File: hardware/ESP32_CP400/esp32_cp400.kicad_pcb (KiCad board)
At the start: 2 copper layers, 110 x 60 mm, 24 parts, among them J2 USB_A, J3 USB_A, J4 USB_A, J5 Micro_SD_Card, J6 Barrel_Jack, J7 DA15_Pins

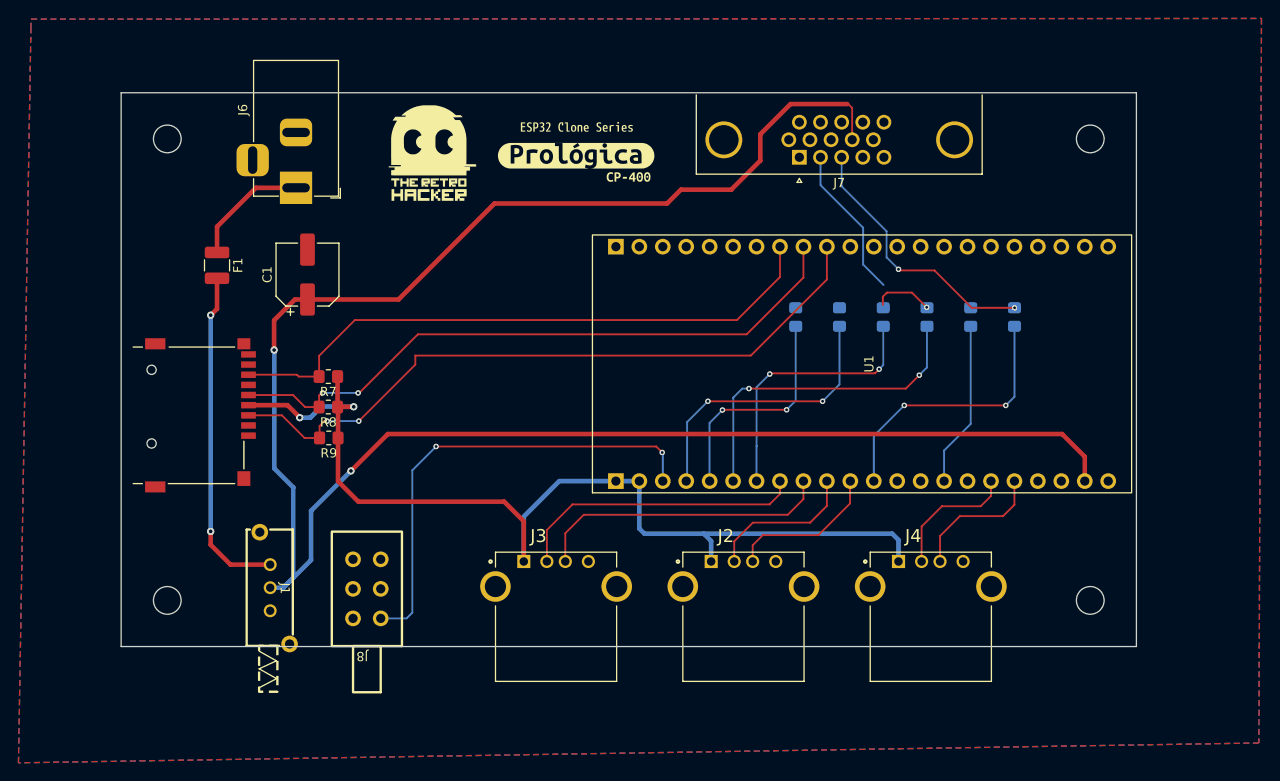
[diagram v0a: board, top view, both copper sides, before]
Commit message: Remove lock files for KiCad projects in ESP32_CP400 directory
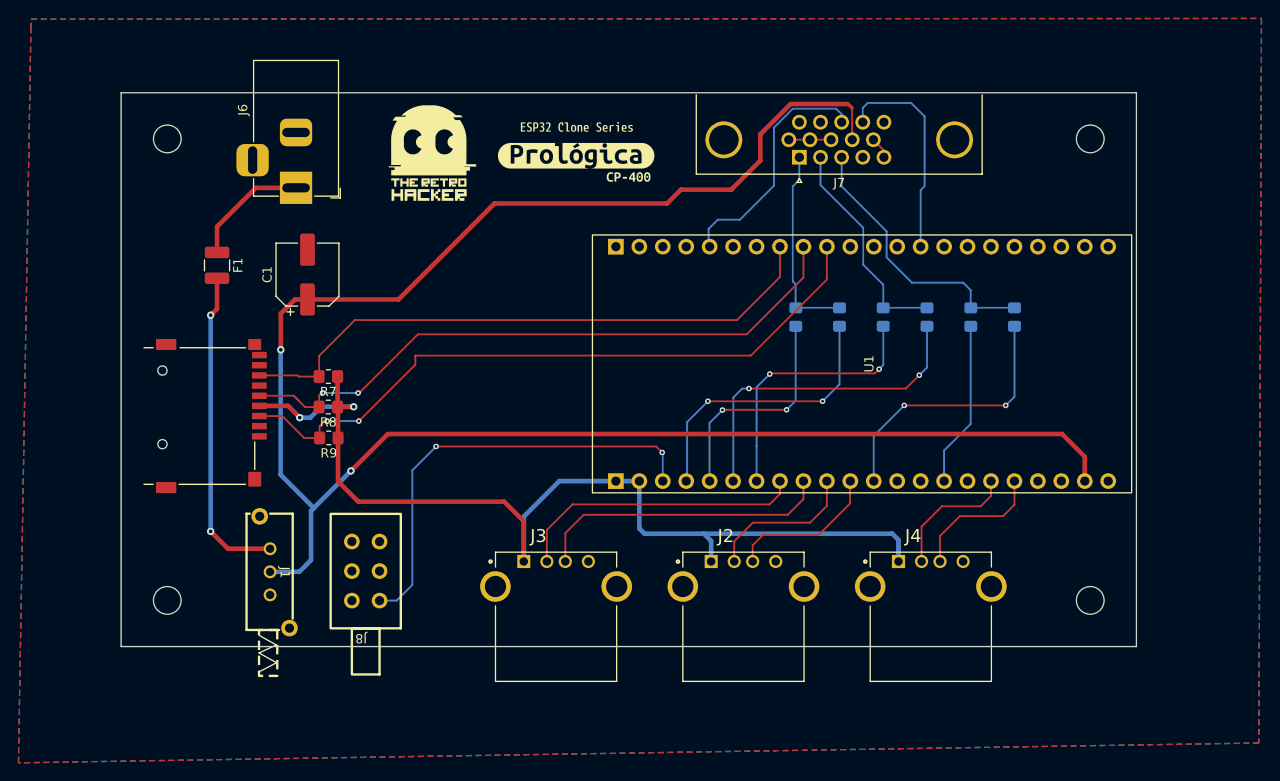
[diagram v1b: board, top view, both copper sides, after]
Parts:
- moved J8 1.93 mm to (116.5, 112.1)
- moved J1 1.72 mm to (106.1, 111.9)
- moved J5 1.18 mm to (94.5, 95.0)
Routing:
- net Net-(J7-P13): track 0.00 -> 26.6 mm
- net Net-(J7-P14): track 0.00 -> 23.4 mm
- net Net-(J7-Pad1): track 0.00 -> 21.5 mm
- net +5V: track 209.8 -> 200.4 mm
- net GND: track 0.00 -> 6.95 mm
- net Net-(U1-RST): track 50.6 -> 48.2 mm
- net Net-(F1-Pad2): track 36.5 -> 34.9 mm
- net Net-(J5-DAT0): track 66.7 -> 65.5 mm
- net Net-(J5-CMD): track 75.7 -> 74.5 mm
- net +3.3V: track 110.4 -> 109.2 mm
- net Net-(J7-Pad3): track 29.0 -> 30.1 mm, vias 2 -> 0
- net Net-(J7-Pad2): track 23.2 -> 23.9 mm, vias 1 -> 0
- net Net-(J5-CLK): track 70.6 -> 70.0 mm
